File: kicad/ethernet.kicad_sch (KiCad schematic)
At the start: 39 parts, among them J2 2.54mm 1x6 Pin Header DIP, J3 2.54mm 1x6 Pin Header DIP, P1 BS-R250210, U2 W5500, Y1 25MHz

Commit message: hierarchical sheet
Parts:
- removed J2: 2.54mm 1x6 Pin Header DIP, IDC-1X6, symbol WIZ850io_SCH_V110-altium-import:root_0_2.54mm 1x6 Pin Header DIP_Scott_lib.IntL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
- removed J3: 2.54mm 1x6 Pin Header DIP, IDC-1X6, symbol WIZ850io_SCH_V110-altium-import:root_0_mirrored_2.54mm 1x6 Pin Header DIP_Scott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
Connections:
- no-connect marks 10 -> 9

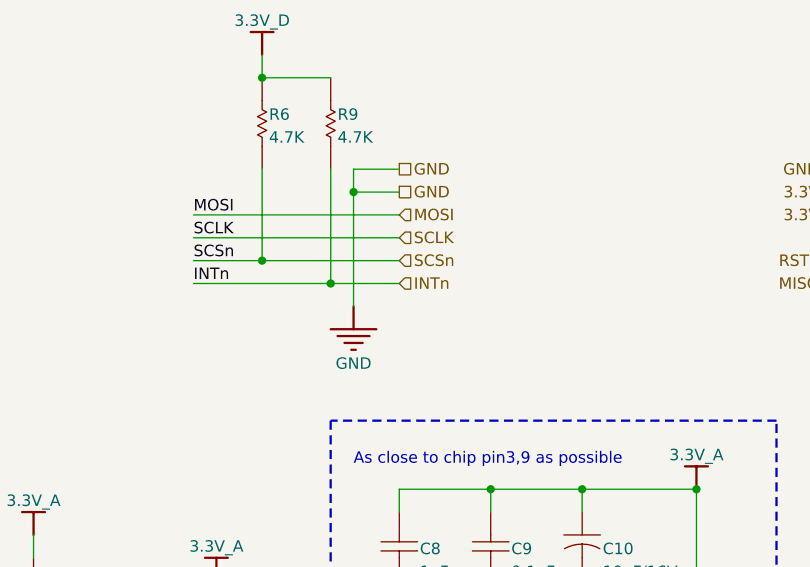
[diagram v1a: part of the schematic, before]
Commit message: finished circuits for rp2040
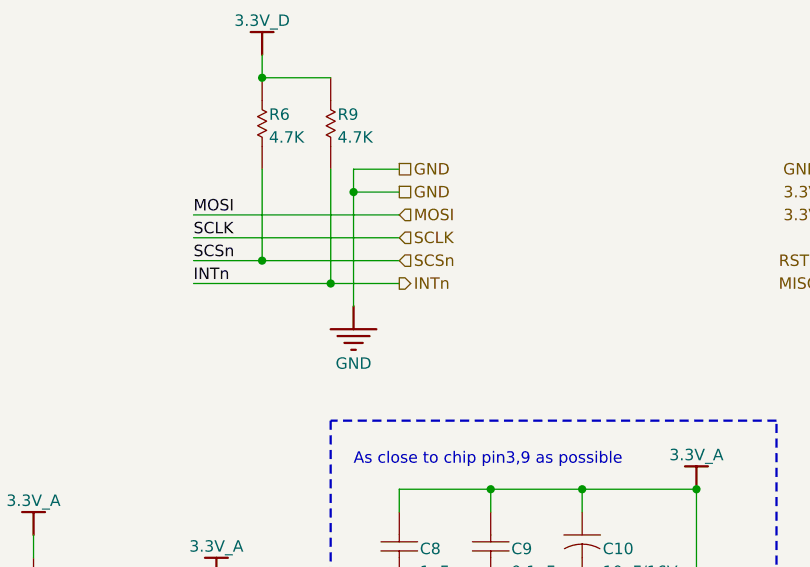
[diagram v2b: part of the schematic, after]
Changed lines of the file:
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@@
 	)
 	(hierarchical_label "INTn"
-		(shape input)
+		(shape output)
 		(at 106.68 53.34 0)
 		(effects
